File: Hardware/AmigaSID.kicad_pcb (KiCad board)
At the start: 2 copper layers, 130 x 67.5 mm, 49 parts, among them CON1 ZorroII, J1 AudioJack3, J2 SID_AUDIO_OUT, J3 SID_AUDIO_IN, J4 12V, J5 GND, Q1 BC547, U1 74HC688, U2 74LS00, U3 SID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

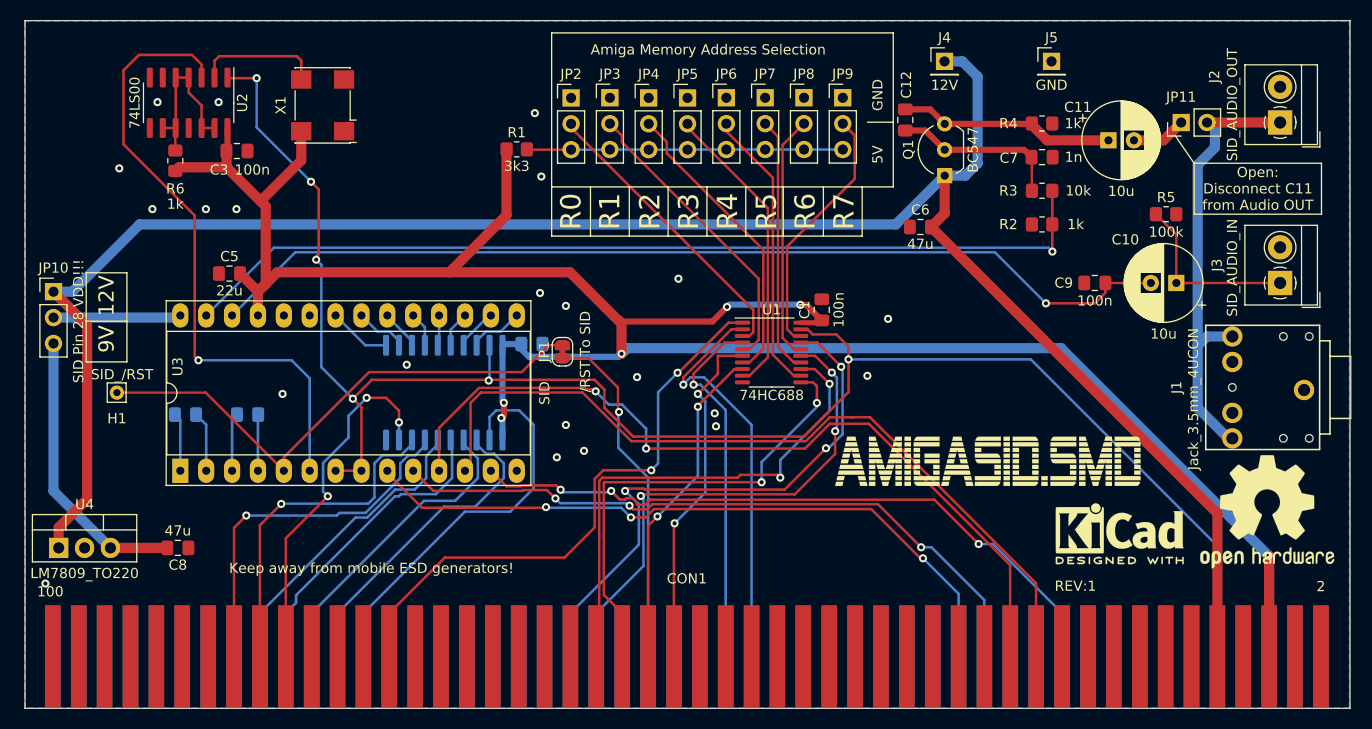
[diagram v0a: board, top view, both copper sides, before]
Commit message: Rev2, moved LDO, reset pin for A4k LED and voltage selection jumper, used only basic parts in JLCPCB bom
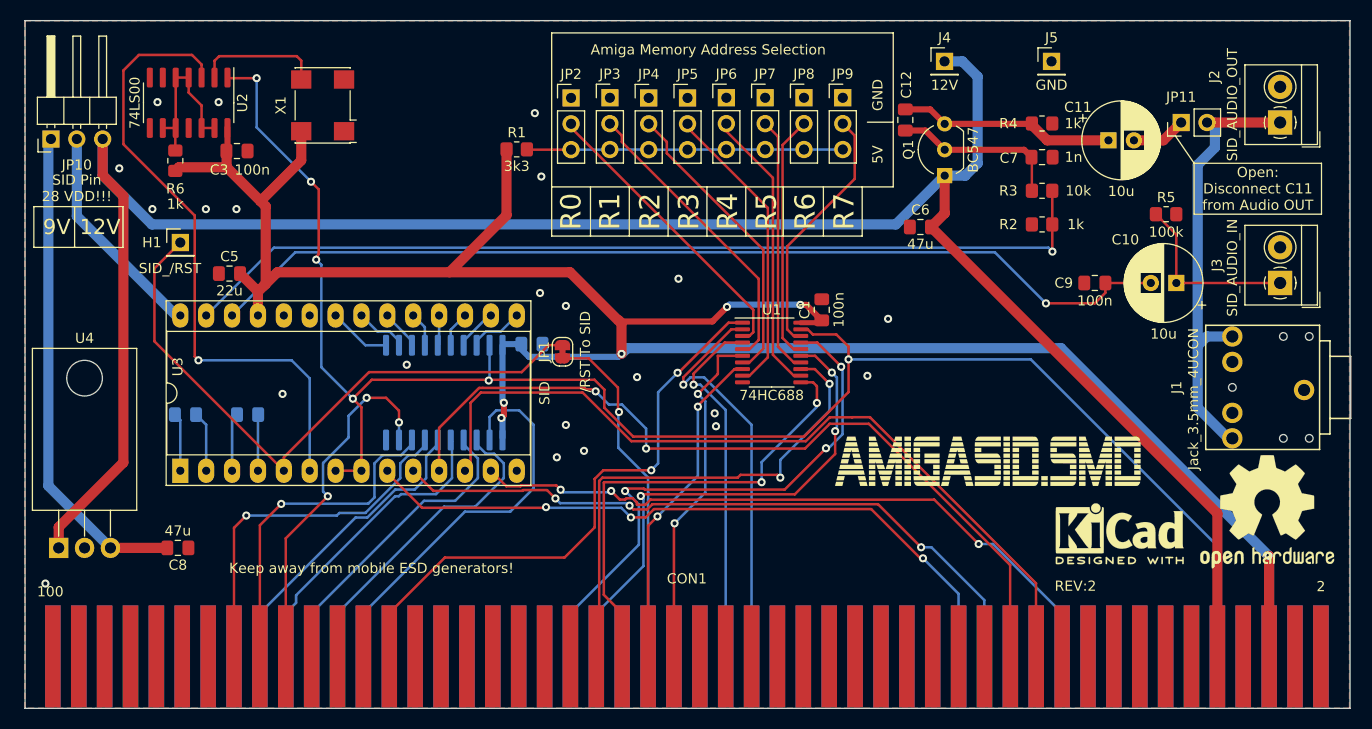
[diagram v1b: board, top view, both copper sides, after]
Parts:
- H1: footprint Connector_Pin:Pin_D0.7mm_L6.5mm_W1.8mm_FlatFork -> Connector_PinHeader_2.54mm:PinHeader_1x01_P2.54mm_Vertical
- JP10: footprint Connector_PinHeader_2.54mm:PinHeader_1x03_P2.54mm_Vertical -> Connector_PinHeader_2.54mm:PinHeader_1x03_P2.54mm_Horizontal
- U4: footprint Package_TO_SOT_THT:TO-220-3_Vertical -> Package_TO_SOT_THT:TO-220-3_Horizontal_TabDown
- moved H1 16.0 mm to (99.1, 89.2)
- moved JP10 15.0 mm to (86.4, 79.0), turned to 90 degrees
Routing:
- net /9v: track 28.0 -> 48.3 mm
- net /12v: track 195.4 -> 209.3 mm
- net /SID_VDD: track 12.2 -> 21.6 mm
- net //RST: track 88.4 -> 97.5 mm
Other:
- board text added: "REV:2"
- board text removed: "REV:1"
